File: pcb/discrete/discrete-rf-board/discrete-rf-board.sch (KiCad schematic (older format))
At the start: 22 parts, among them J101 SMA, U101 BGS12PL6E6327XTSA1, U102 BGS12PL6E6327XTSA1

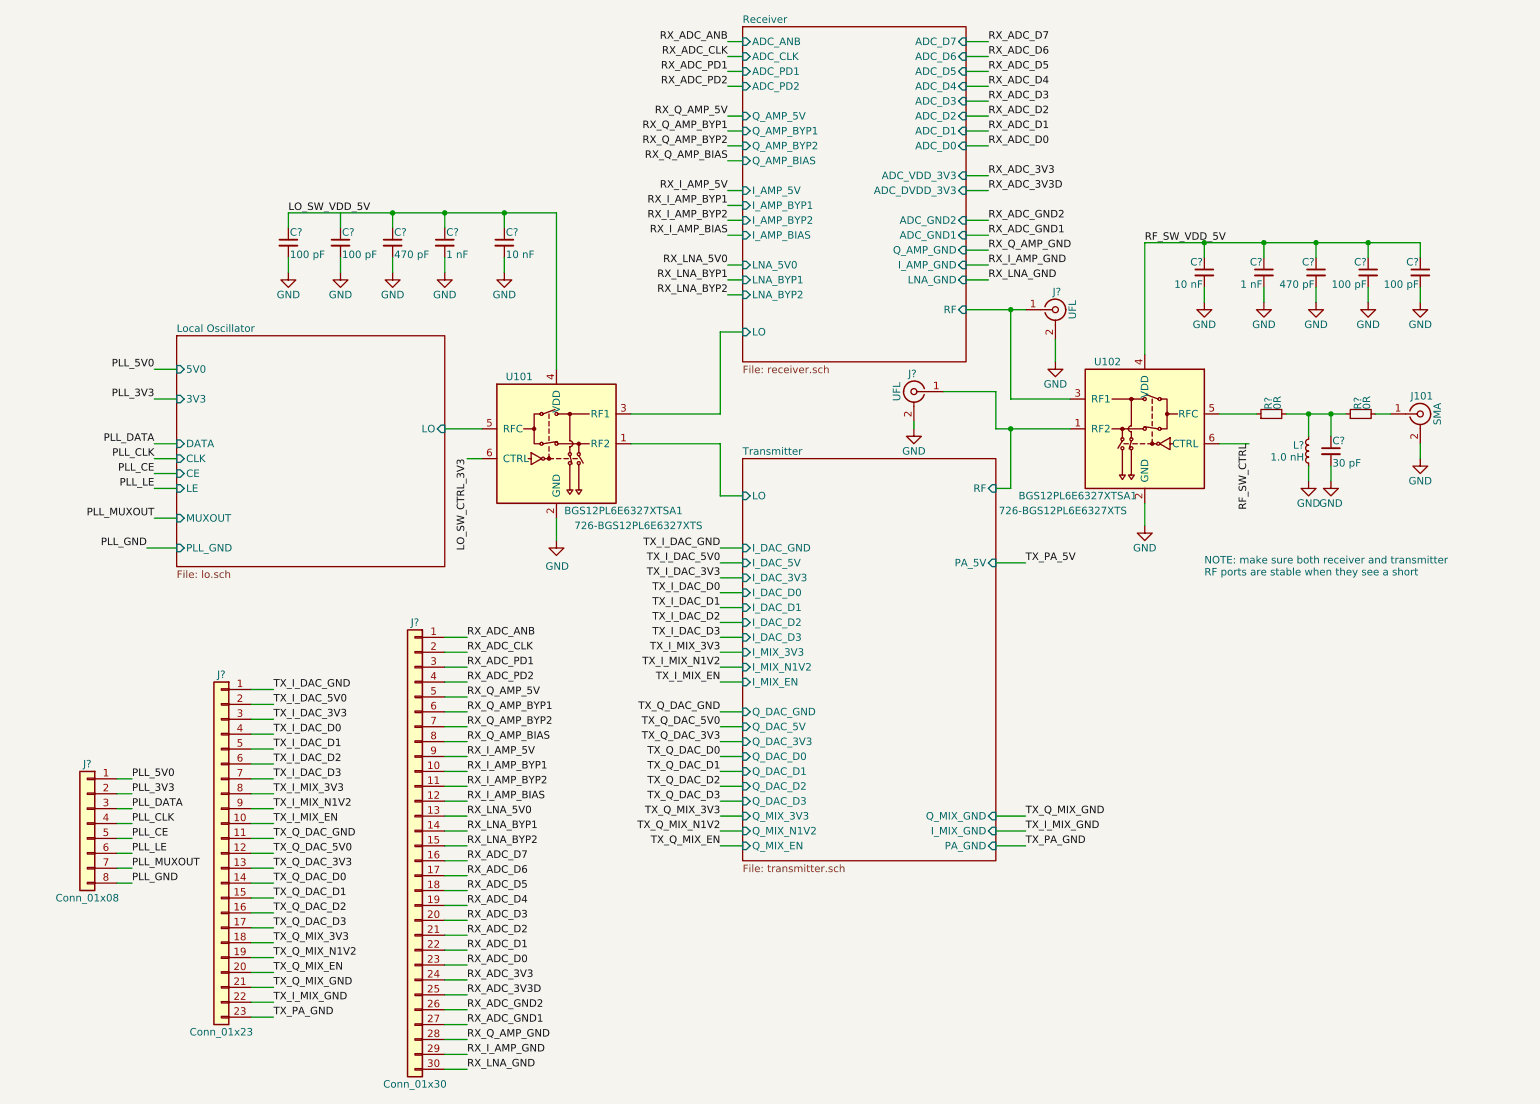
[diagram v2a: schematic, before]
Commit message: Start work in footprinting everything
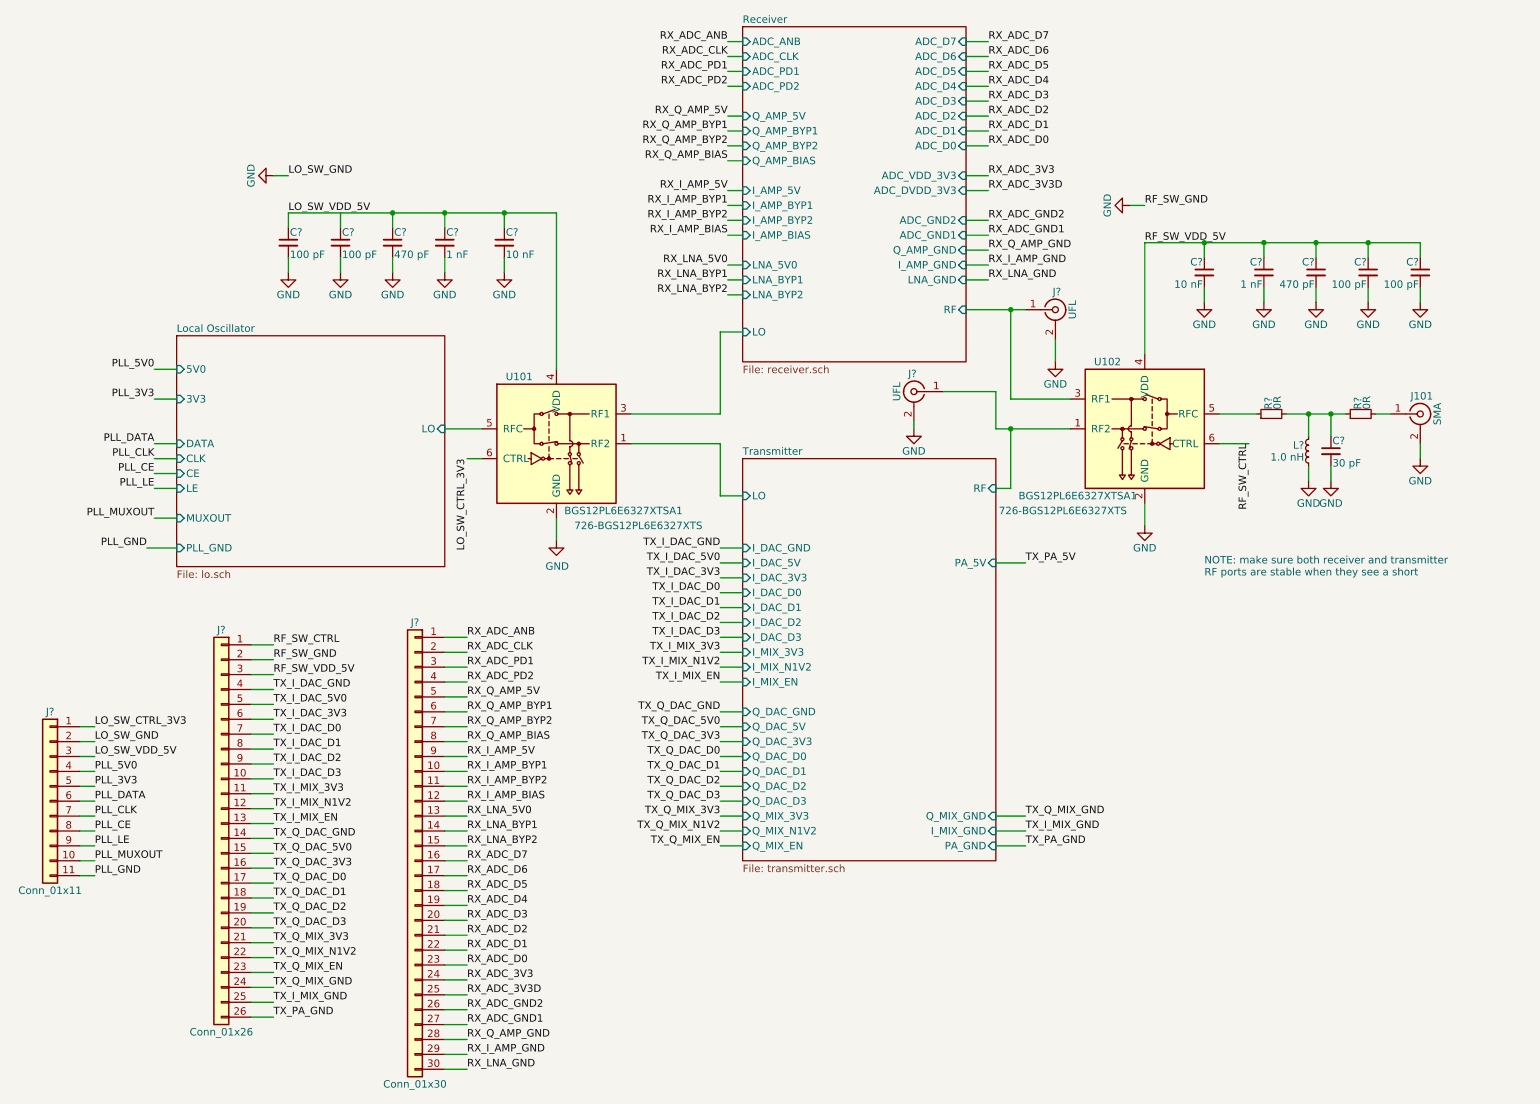
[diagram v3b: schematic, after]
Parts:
- removed J?: Conn_01x08, symbol Connector_Generic:Conn_01x08
- removed J?: Conn_01x23, symbol Connector_Generic:Conn_01x23
- added J?: Conn_01x11, symbol Connector_Generic:Conn_01x11
- added J?: Conn_01x26, symbol Connector_Generic:Conn_01x26
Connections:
- net GND: now also J?.2 (Pin_2), J?.2 (Pin_2)
- net LO_SW_CTRL_3V3: now also J?.1 (Pin_1)
- net LO_SW_VDD_5V: now also J?.3 (Pin_3)
- net PLL_3V3: now also J?.5 (Pin_5)
- net PLL_5V0: now also J?.4 (Pin_4)
- net PLL_CE: now also J?.8 (Pin_8)
- net PLL_CLK: now also J?.7 (Pin_7)
- net PLL_DATA: now also J?.6 (Pin_6)
- net PLL_GND: now also J?.11 (Pin_11)
- net PLL_LE: now also J?.9 (Pin_9)
- net PLL_MUXOUT: now also J?.10 (Pin_10)
- net RF_SW_CTRL: now also J?.1 (Pin_1)
- net RF_SW_VDD_5V: now also J?.3 (Pin_3)
- net TX_I_DAC_3V3: now also J?.6 (Pin_6)
- net TX_I_DAC_5V0: now also J?.5 (Pin_5)
- net TX_I_DAC_D0: now also J?.7 (Pin_7)
- net TX_I_DAC_D1: now also J?.8 (Pin_8)
- net TX_I_DAC_D2: now also J?.9 (Pin_9)
- net TX_I_DAC_D3: now also J?.10 (Pin_10)
- net TX_I_DAC_GND: now also J?.4 (Pin_4)
- net TX_I_MIX_3V3: now also J?.11 (Pin_11)
- net TX_I_MIX_EN: now also J?.13 (Pin_13)
- net TX_I_MIX_GND: now also J?.25 (Pin_25)
- net TX_I_MIX_N1V2: now also J?.12 (Pin_12)
- net TX_PA_GND: now also J?.26 (Pin_26)
- net TX_Q_DAC_3V3: now also J?.16 (Pin_16)
- net TX_Q_DAC_5V0: now also J?.15 (Pin_15)
- net TX_Q_DAC_D0: now also J?.17 (Pin_17)
- net TX_Q_DAC_D1: now also J?.18 (Pin_18)
- net TX_Q_DAC_D2: now also J?.19 (Pin_19)
- net TX_Q_DAC_D3: now also J?.20 (Pin_20)
- net TX_Q_DAC_GND: now also J?.14 (Pin_14)
- net TX_Q_MIX_3V3: now also J?.21 (Pin_21)
- net TX_Q_MIX_EN: now also J?.23 (Pin_23)
- net TX_Q_MIX_GND: now also J?.24 (Pin_24)
- net TX_Q_MIX_N1V2: now also J?.22 (Pin_22)
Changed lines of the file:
@@
 Wire Wire Line
 	3750 3550 3850 3550
-Text Label 9000 3450 3    50   ~ 0
-RF_SW_CTRL
 Wire Wire Line
 	9000 3450 8800 3450
@@
 Wire Wire Line
 	7250 2350 7100 2350
-Text Label 1500 5700 0    50   ~ 0
+Text Label 1250 5650 0    50   ~ 0
 PLL_5V0
-Text Label 1500 5800 0    50   ~ 0
+Text Label 1250 5750 0    50   ~ 0
 PLL_3V3
-Text Label 1500 5900 0    50   ~ 0
+Text Label 1250 5850 0    50   ~ 0
 PLL_DATA
-Text Label 1500 6000 0    50   ~ 0
+Text Label 1250 5950 0    50   ~ 0
 PLL_CLK
-Text Label 1500 6100 0    50   ~ 0
+Text Label 1250 6050 0    50   ~ 0
 PLL_CE
-Text Label 1500 6200 0    50   ~ 0
+Text Label 1250 6150 0    50   ~ 0
 PLL_LE
-Text Label 1500 6300 0    50   ~ 0
+Text Label 1250 6250 0    50   ~ 0
 PLL_MUXOUT
-Text Label 1500 6400 0    50   ~ 0
+Text Label 1250 6350 0    50   ~ 0
 PLL_GND
 Text Label 2450 5100 0    50   ~ 0
@@
 Text Label 3750 6150 0    50   ~ 0
 RX_LNA_BYP2
-$Comp
-L Connector_Generic:Conn_01x08 J?
-U 1 1 5DA33260
-P 1200 6000
-F 0 "J?" H 1200 6400 50  0000 C CNN
-F 1 "Conn_01x08" H 1200 5500 50  0000 C CNN
-F 2 "" H 1200 6000 50  0001 C CNN
-F 3 "~" H 1200 6000 50  0001 C CNN
-	1    1200 6000
-	-1   0    0    -1
-$EndComp
-Wire Wire Line
-	1400 5700 1500 5700
-Wire Wire Line
-	1500 5800 1400 5800
-Wire Wire Line
-	1400 5900 1500 5900
-Wire Wire Line
-	1500 6000 1400 6000
-Wire Wire Line
-	1400 6100 1500 6100
-Wire Wire Line
-	1500 6200 1400 6200
-Wire Wire Line
-	1400 6300 1500 6300
-Wire Wire Line
-	1400 6400 1500 6400
+Wire Wire Line
+	1150 5650 1250 5650
+Wire Wire Line
+	1250 5750 1150 5750
+Wire Wire Line
+	1150 5850 1250 5850
+Wire Wire Line
+	1250 5950 1150 5950
+Wire Wire Line
+	1150 6050 1250 6050
+Wire Wire Line
+	1250 6150 1150 6150
+Wire Wire Line
+	1150 6250 1250 6250
+Wire Wire Line
+	1150 6350 1250 6350
 Wire Wire Line
 	2450 5100 2300 5100
@@
 Wire Wire Line
 	2300 6300 2450 6300
-$Comp
-L Connector_Generic:Conn_01x23 J?
-U 1 1 5DAC4901
-P 2100 6200
-F 0 "J?" H 2100 7400 50  0000 C CNN
-F 1 "Conn_01x23" H 2100 5000 50  0000 C CNN
-F 2 "" H 2100 6200 50  0001 C CNN
-F 3 "~" H 2100 6200 50  0001 C CNN
-	1    2100 6200
-	-1   0    0    -1
-$EndComp
 $Comp
 L Connector_Generic:Conn_01x30 J?
@@
 Wire Wire Line
 	3600 7450 3750 7450
+Text Label 2450 5000 0    50   ~ 0
+RF_SW_VDD_5V
+Text Label 1250 5550 0    50   ~ 0
+LO_SW_VDD_5V
+Wire Wire Line
+	1150 5550 1250 5550
+Text Label 8300 1850 0    50   ~ 0
+RF_SW_GND
+$Comp
+L power:GND #PWR?
+U 1 1 5DB60E45
+P 8200 1850
+F 0 "#PWR?" H 8200 1600 50  0001 C CNN
+F 1 "GND" H 8200 1700 50  0000 C CNN
+F 2 "" H 8200 1850 50  0001 C CNN
+F 3 "" H 8200 1850 50  0001 C CNN
+	1    8200 1850
+	0    1    1    0
+$EndComp
+Wire Wire Line
+	8200 1850 8300 1850
+Text Label 2450 4900 0    50   ~ 0
+RF_SW_GND
+Wire Wire Line
+	2300 5000 2450 5000
+Wire Wire Line
+	2450 4900 2300 4900
+Text Label 2550 1650 0    50   ~ 0
+LO_SW_GND
+$Comp
+L power:GND #PWR?
+U 1 1 5DB9787B
+P 2450 1650
+F 0 "#PWR?" H 2450 1400 50  0001 C CNN
+F 1 "GND" H 2450 1500 50  0000 C CNN
+F 2 "" H 2450 1650 50  0001 C CNN
+F 3 "" H 2450 1650 50  0001 C CNN
+	1    2450 1650
+	0    1    1    0
+$EndComp
+Wire Wire Line
+	2450 1650 2550 1650
+Text Label 1250 5450 0    50   ~ 0
+LO_SW_GND
+Wire Wire Line
+	1150 5450 1250 5450
+Text Label 1250 5350 0    50   ~ 0
+LO_SW_CTRL_3V3
+Text Label 9000 3450 3    50   ~ 0
+RF_SW_CTRL
+Text Label 2450 4800 0    50   ~ 0
+RF_SW_CTRL
+$Comp
+L Connector_Generic:Conn_01x11 J?
+U 1 1 5DBBF0DF
+P 950 5850
+F 0 "J?" H 950 6450 50  0000 C CNN
+F 1 "Conn_01x11" H 950 5250 50  0000 C CNN
+F 2 "" H 950 5850 50  0001 C CNN
+F 3 "~" H 950 5850 50  0001 C CNN
+	1    950  5850
+	-1   0    0    -1
+$EndComp
+$Comp
+L Connector_Generic:Conn_01x26 J?
+U 1 1 5DBC1FAA
+P 2100 6000
+F 0 "J?" H 2100 7300 50  0000 C CNN
+F 1 "Conn_01x26" H 2100 4600 50  0000 C CNN
+F 2 "" H 2100 6000 50  0001 C CNN
+F 3 "~" H 2100 6000 50  0001 C CNN
+	1    2100 6000
+	-1   0    0    -1
+$EndComp
+Wire Wire Line
+	2300 4800 2450 4800
+Wire Wire Line
+	1150 5350 1250 5350
 $EndSCHEMATC

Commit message: The footprintening continues
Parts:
- J101: footprint (none) -> discrete_footprints:142-0701-801-with-taper; Mouser (none) -> 530-142-0701-801
- J?: footprint (none) -> discrete_footprints:2337019-1; Mouser (none) -> 571-2337019-1
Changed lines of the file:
@@
 F 0 "J101" H 10160 3370 50  0000 C CNN
 F 1 "SMA" V 10265 3250 50  0000 C CNN
-F 2 "" H 10150 3250 50  0001 C CNN
+F 2 "discrete_footprints:142-0701-801-with-taper" H 10150 3250 50  0001 C CNN
 F 3 " ~" H 10150 3250 50  0001 C CNN
+F 4 " 530-142-0701-801 " H 10150 3250 50  0001 C CNN "Mouser"
 	1    10150 3250
 	1    0    0    -1
@@
 F 0 "J?" H 6760 3220 50  0000 C CNN
 F 1 "UFL" V 6865 3100 50  0000 C CNN
-F 2 "" H 6750 3100 50  0001 C CNN
+F 2 "discrete_footprints:2337019-1" H 6750 3100 50  0001 C CNN
 F 3 " ~" H 6750 3100 50  0001 C CNN
+F 4 " 571-2337019-1" H 6750 3100 50  0001 C CNN "Mouser"
 	1    6750 3100
 	-1   0    0    -1

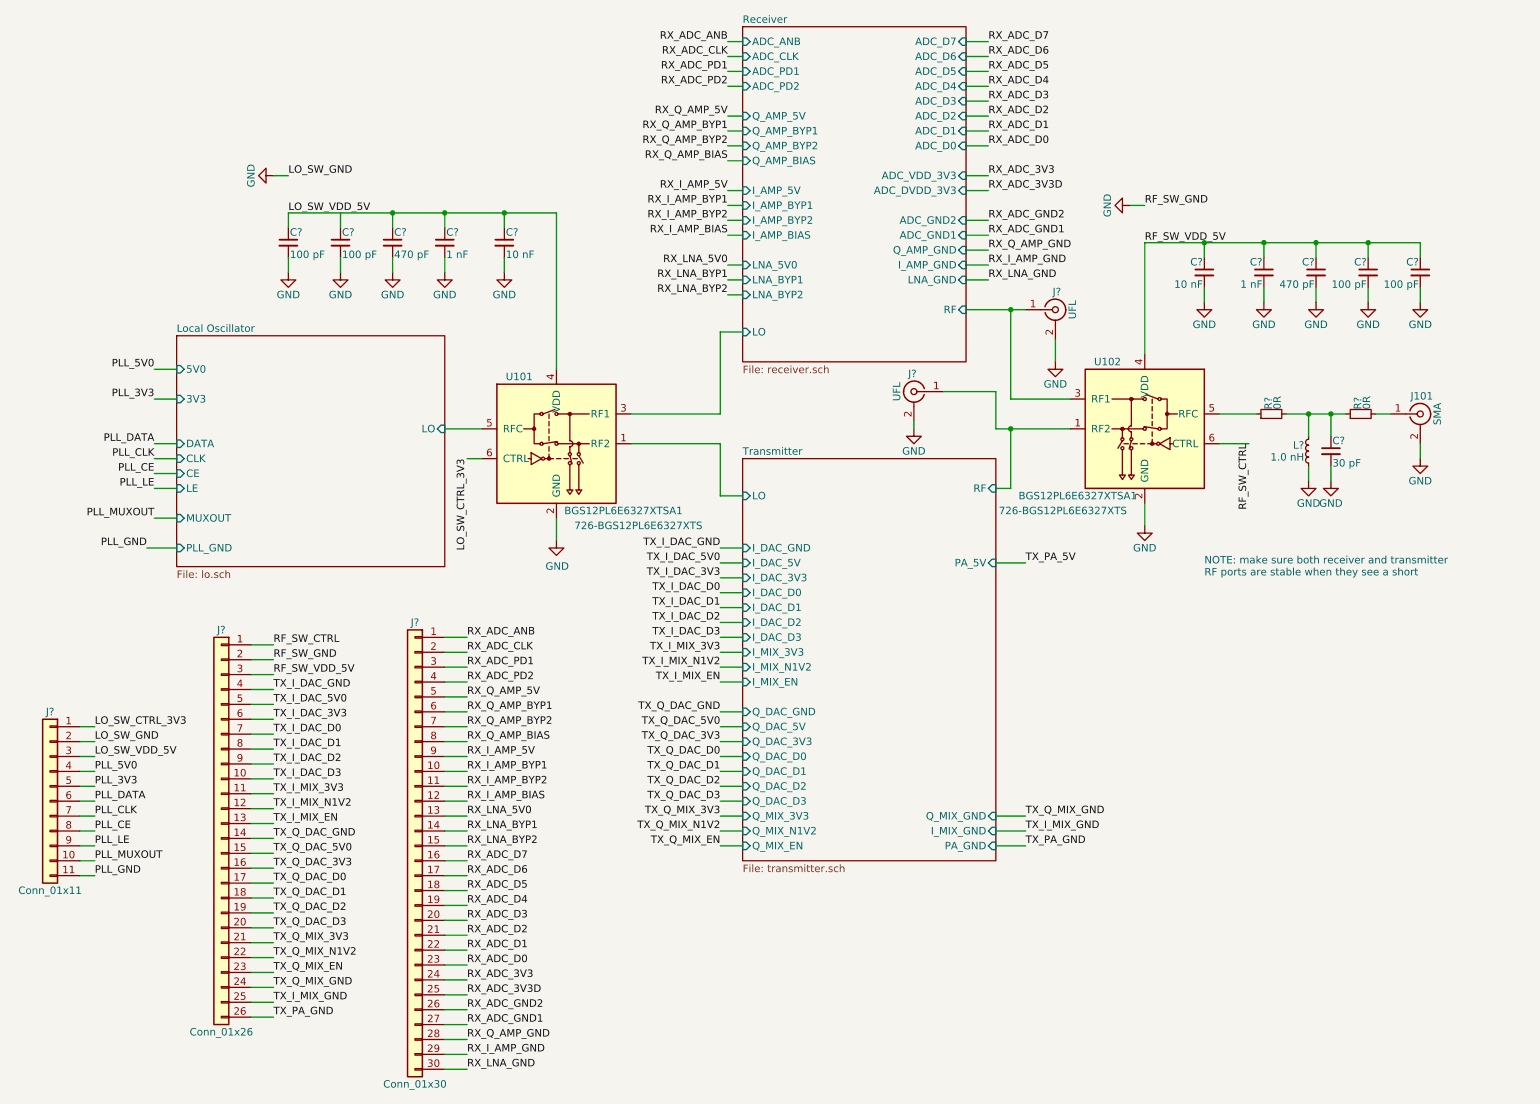
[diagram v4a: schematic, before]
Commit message: Add matching PNP/NPN transistor pairs, fix pin numbering for BFU520R transistors TODO fix biasing on power stage, source last NPN transistor, autofill and start sourcing passives
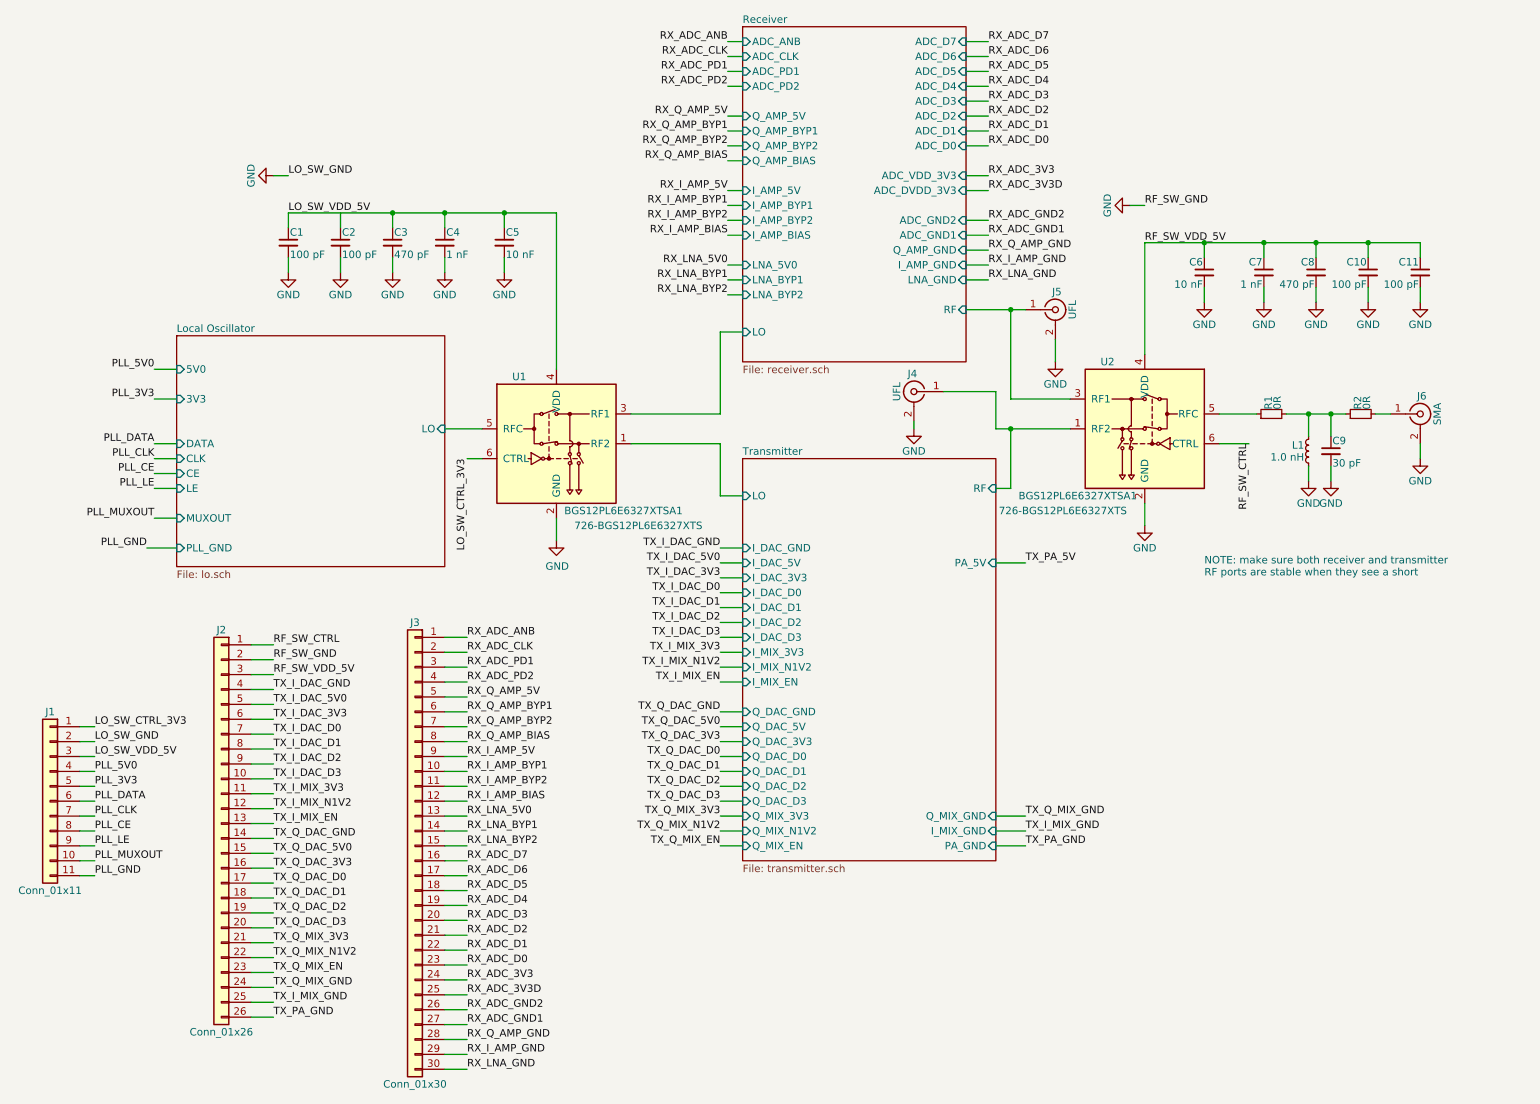
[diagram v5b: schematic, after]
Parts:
- gave numbers to parts that had none: 19
- renumbered J101 to J6, U101 to U1, U102 to U2

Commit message: Autofill; lots left to do
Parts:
- J5: footprint (none) -> discrete_footprints:2337019-1; Mouser (none) -> 571-2337019-1
- U1, U2: footprint (none) -> discrete_footprints:Infineon_TSLP-6-4
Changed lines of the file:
@@
 F 0 "U1" H 4100 3900 50  0000 C CNN
 F 1 "BGS12PL6E6327XTSA1" H 4800 3000 50  0000 C CNN
-F 2 "" H 4350 3450 50  0001 C CNN
+F 2 "discrete_footprints:Infineon_TSLP-6-4" H 4350 3450 50  0001 C CNN
 F 3 "" H 4350 3450 50  0001 C CNN
 F 4 "726-BGS12PL6E6327XTS" H 4900 2900 50  0000 C CNN "Mouser"
@@
 F 0 "U2" H 8550 3800 50  0000 C CNN
 F 1 "BGS12PL6E6327XTSA1" H 8750 2900 50  0000 C CNN
-F 2 "" H 8300 3350 50  0001 C CNN
+F 2 "discrete_footprints:Infineon_TSLP-6-4" H 8300 3350 50  0001 C CNN
 F 3 "" H 8300 3350 50  0001 C CNN
 F 4 "726-BGS12PL6E6327XTS" H 8850 2800 50  0000 C CNN "Mouser"
@@
 F 0 "J5" H 7710 2670 50  0000 C CNN
 F 1 "UFL" V 7815 2550 50  0000 C CNN
-F 2 "" H 7700 2550 50  0001 C CNN
+F 2 "discrete_footprints:2337019-1" H 7700 2550 50  0001 C CNN
 F 3 " ~" H 7700 2550 50  0001 C CNN
+F 4 " 571-2337019-1" H 7700 2550 50  0001 C CNN "Mouser"
 	1    7700 2550
 	1    0    0    -1

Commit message: Footprint some stuff
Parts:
- R1: footprint (none) -> Capacitor_SMD:C_0402_1005Metric; Mouser (none) -> 71-CRCW04020000Z0EDC
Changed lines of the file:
@@
 F 0 "R1" H 9180 3270 50  0000 L CNN
 F 1 "0R" H 9180 3210 50  0000 L CNN
-F 2 "" H 9150 3250 50  0001 C CNN
+F 2 "Capacitor_SMD:C_0402_1005Metric" H 9150 3250 50  0001 C CNN
 F 3 "~" H 9150 3250 50  0001 C CNN
+F 4 "71-CRCW04020000Z0EDC" H 9150 3250 50  0001 C CNN "Mouser"
 	1    9150 3250
 	0    -1   -1   0
